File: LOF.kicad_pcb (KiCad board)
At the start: 2 copper layers, 29 parts, among them IC10 PEL12D-4225S-S1024, IC11 PEL12D-4225S-S1024, IC12 PEL12D-4225S-S1024, IC13 PEL12D-4225S-S1024, IC14 PEL12D-4225S-S1024, IC15 PEL12D-4225S-S1024, IC16 PEL12D-4225S-S1024, IC9 PEL12D-4225S-S1024

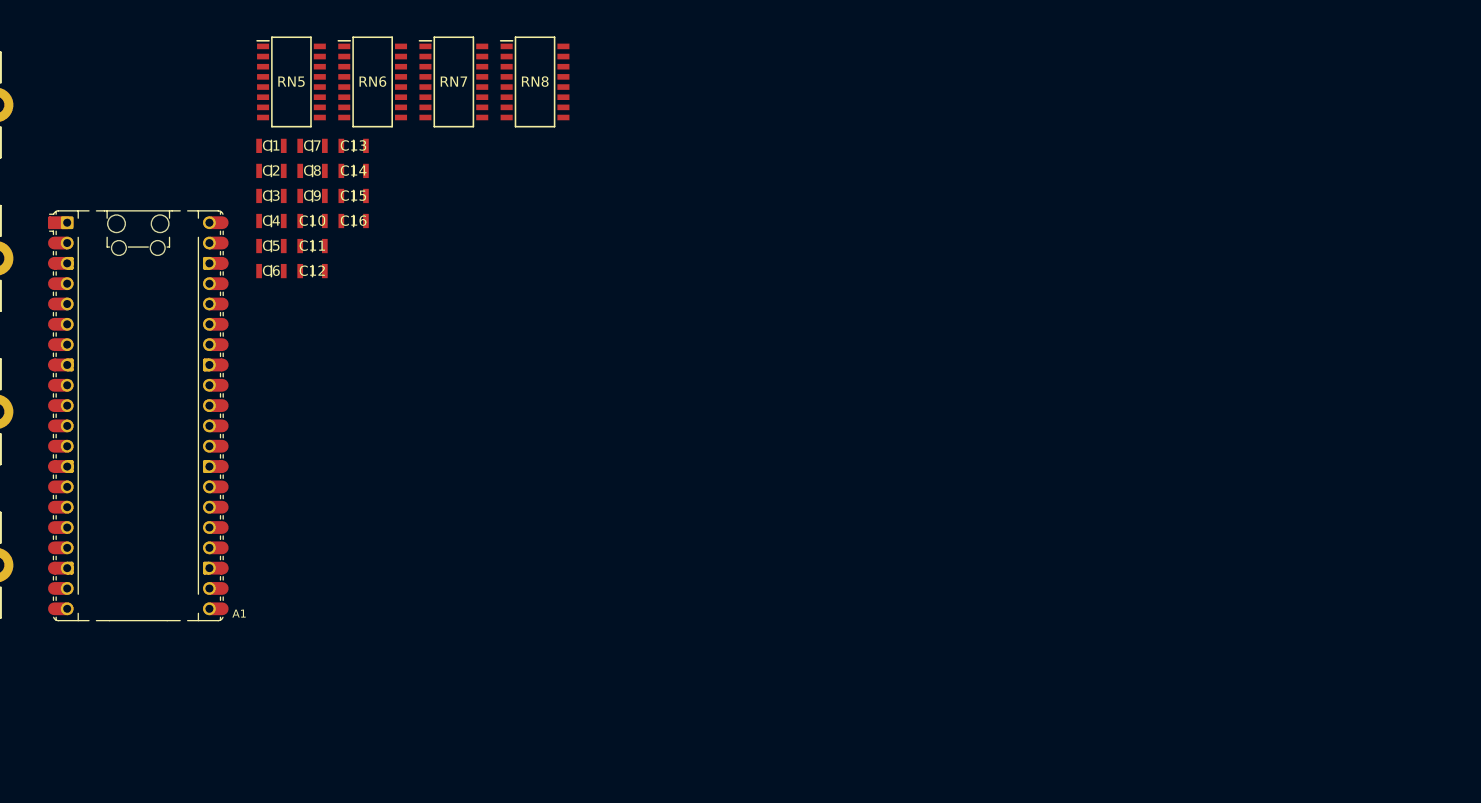
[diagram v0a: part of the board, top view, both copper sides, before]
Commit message: Added variable resistor and switches
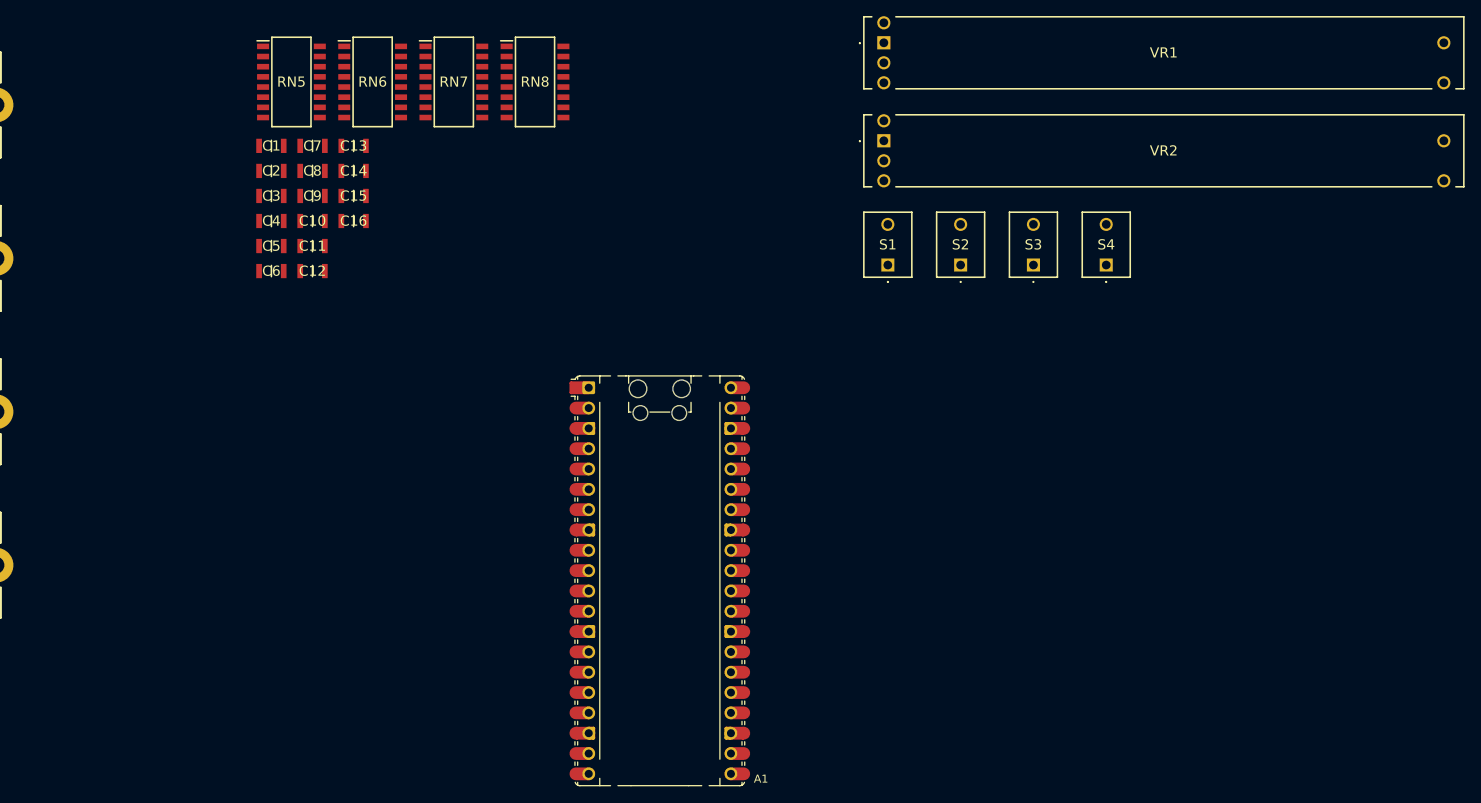
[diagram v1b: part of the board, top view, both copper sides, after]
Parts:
- added S1: 2MS6T1B3M2QES, SamacSys_Parts:2MS6T1B3M2QES, F.Cu at (196.5, 66.5)
- added S2: 2MS6T1B3M2QES, SamacSys_Parts:2MS6T1B3M2QES, F.Cu at (205.6, 66.5)
- added S3: 2MS6T1B3M2QES, SamacSys_Parts:2MS6T1B3M2QES, F.Cu at (214.7, 66.5)
- added S4: 2MS6T1B3M2QES, SamacSys_Parts:2MS6T1B3M2QES, F.Cu at (223.8, 66.5)
- added VR1: PTL60-15O1-104B2, SamacSys_Parts:PTL6015O1104B2, F.Cu at (196.0, 38.8)
- added VR2: PTL60-15O1-104B2, SamacSys_Parts:PTL6015O1104B2, F.Cu at (196.0, 51.0)
- moved A1 68.4 mm to (168.0, 106.0)
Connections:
- net 5V renamed /RC Filtered Encoders/5V
- IC10 pad 1: unconnected-(IC10---Pad1) -> GND
- IC10 pad 2: unconnected-(IC10-+_1-Pad2) -> /RC Filtered Encoders/E5_LED_BLUE
- IC10 pad 3: unconnected-(IC10-+_2-Pad3) -> /RC Filtered Encoders/E5_LED_ORANGE
- IC10 pad 4: unconnected-(IC10-COM-Pad4) -> /RC Filtered Encoders/E5_SW
- IC11 pad 1: unconnected-(IC11---Pad1) -> GND
- IC11 pad 2: unconnected-(IC11-+_1-Pad2) -> /RC Filtered Encoders/E2_LED_BLUE
- IC11 pad 3: unconnected-(IC11-+_2-Pad3) -> /RC Filtered Encoders/E2_LED_ORANGE
- IC11 pad 4: unconnected-(IC11-COM-Pad4) -> /RC Filtered Encoders/E2_SW
- IC12 pad 1: unconnected-(IC12---Pad1) -> GND
- IC12 pad 2: unconnected-(IC12-+_1-Pad2) -> /RC Filtered Encoders/E6_LED_BLUE
- IC12 pad 3: unconnected-(IC12-+_2-Pad3) -> /RC Filtered Encoders/E6_LED_ORANGE
- IC12 pad 4: unconnected-(IC12-COM-Pad4) -> /RC Filtered Encoders/E6_SW
- IC13 pad 1: unconnected-(IC13---Pad1) -> GND
- IC13 pad 2: unconnected-(IC13-+_1-Pad2) -> /RC Filtered Encoders/E3_LED_BLUE
- IC13 pad 3: unconnected-(IC13-+_2-Pad3) -> /RC Filtered Encoders/E3_LED_ORANGE
- IC13 pad 4: unconnected-(IC13-COM-Pad4) -> /RC Filtered Encoders/E3_SW
- IC14 pad 1: unconnected-(IC14---Pad1) -> GND
- IC14 pad 2: unconnected-(IC14-+_1-Pad2) -> /RC Filtered Encoders/E7_LED_BLUE
- IC14 pad 3: unconnected-(IC14-+_2-Pad3) -> /RC Filtered Encoders/E7_LED_ORANGE
- IC14 pad 4: unconnected-(IC14-COM-Pad4) -> /RC Filtered Encoders/E7_SW
- IC15 pad 1: unconnected-(IC15---Pad1) -> GND
- IC15 pad 2: unconnected-(IC15-+_1-Pad2) -> /RC Filtered Encoders/E4_LED_BLUE
- IC15 pad 3: unconnected-(IC15-+_2-Pad3) -> /RC Filtered Encoders/E4_LED_ORANGE
- IC15 pad 4: unconnected-(IC15-COM-Pad4) -> /RC Filtered Encoders/E4_SW
- IC16 pad 1: unconnected-(IC16---Pad1) -> GND
- IC16 pad 2: unconnected-(IC16-+_1-Pad2) -> /RC Filtered Encoders/E8_LED_BLUE
- IC16 pad 3: unconnected-(IC16-+_2-Pad3) -> /RC Filtered Encoders/E8_LED_ORANGE
- IC16 pad 4: unconnected-(IC16-COM-Pad4) -> /RC Filtered Encoders/E8_SW
- IC9 pad 1: unconnected-(IC9---Pad1) -> GND
- IC9 pad 2: unconnected-(IC9-+_1-Pad2) -> /RC Filtered Encoders/E1_LED_BLUE
- IC9 pad 3: unconnected-(IC9-+_2-Pad3) -> /RC Filtered Encoders/E1_LED_ORANGE
- IC9 pad 4: unconnected-(IC9-COM-Pad4) -> /RC Filtered Encoders/E1_SW

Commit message: Update schematic
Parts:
- added J1: EXT_3.3V, Connector_Wire:SolderWire-0.75sqmm_1x01_D1.25mm_OD3.5mm_Relief, F.Cu at (61.7, 160.7)
- added J2: VBUS_IN, Connector_Wire:SolderWire-0.75sqmm_1x01_D1.25mm_OD3.5mm_Relief, F.Cu at (67.7, 160.7)
- added J3: GND, Connector_Wire:SolderWire-0.75sqmm_1x01_D1.25mm_OD3.5mm_Relief, F.Cu at (73.8, 160.7)
- added U1: 815, Kicad Libs:MODULE_815, F.Cu at (90.6, 144.5)
- C1, C10, C11, C12, C13, C14, C15, C16, C2, C3, C4, C5, C6, C7, C8, C9: footprint SamacSys_Parts:CAPC3216X90N -> Kicad Libs:CAPC3216X90N
- IC10, IC11, IC12, IC13, IC14, IC15, IC16, IC9: footprint SamacSys_Parts:PEL12D4225SS1024 -> Kicad Libs:PEL12D4225SS1024
- S1, S2, S3, S4: footprint SamacSys_Parts:2MS6T1B3M2QES -> Kicad Libs:2MS6T1B3M2QES
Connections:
- net /RC Filtered Encoders/5V renamed /RC Filtered Encoders/3.3V
- net /RC Filtered Encoders/E1_SW renamed /E1_SW
- net /RC Filtered Encoders/E2_SW renamed /E2_SW
- net /RC Filtered Encoders/E3_SW renamed /E3_SW
- net /RC Filtered Encoders/E4_SW renamed /E4_SW
- net /RC Filtered Encoders/E5_SW renamed /E5_SW
- net /RC Filtered Encoders/E6_SW renamed /E6_SW
- net /RC Filtered Encoders/E7_SW renamed /E7_SW
- net /RC Filtered Encoders/E8_SW renamed /E8_SW
- A1 pad 1: unconnected-(A1-GPIO0-Pad1) -> /AOut1
- A1 pad 10: unconnected-(A1-GPIO7-Pad10) -> /BOut3
- A1 pad 11: unconnected-(A1-GPIO8-Pad11) -> /AOut4
- A1 pad 12: unconnected-(A1-GPIO9-Pad12) -> /BOut4
- A1 pad 14: unconnected-(A1-GPIO10-Pad14) -> /AOut5
- A1 pad 15: unconnected-(A1-GPIO11-Pad15) -> /BOut5
- A1 pad 16: unconnected-(A1-GPIO12-Pad16) -> /AOut6
- A1 pad 17: unconnected-(A1-GPIO13-Pad17) -> /BOut6
- A1 pad 19: unconnected-(A1-GPIO14-Pad19) -> /AOut7
- A1 pad 2: unconnected-(A1-GPIO1-Pad2) -> /BOut1
- A1 pad 20: unconnected-(A1-GPIO15-Pad20) -> /BOut7
- A1 pad 21: unconnected-(A1-GPIO16-Pad21) -> /AOut8
- A1 pad 22: unconnected-(A1-GPIO17-Pad22) -> /BOut8
- A1 pad 24: unconnected-(A1-GPIO18-Pad24) -> /S1_NC
- A1 pad 25: unconnected-(A1-GPIO19-Pad25) -> /S2_NC
- A1 pad 26: unconnected-(A1-GPIO20-Pad26) -> /S3_NC
- A1 pad 27: unconnected-(A1-GPIO21-Pad27) -> /S4_NC
- A1 pad 31: unconnected-(A1-GPIO26_ADC0-Pad31) -> /WIPER_VR1
- A1 pad 32: unconnected-(A1-GPIO27_ADC1-Pad32) -> /WIPER_VR2
- A1 pad 36: unconnected-(A1-3V3-Pad36) -> /3V3
- A1 pad 4: unconnected-(A1-GPIO2-Pad4) -> /AOut2
- A1 pad 40: unconnected-(A1-VBUS-Pad40) -> /VBUS
- A1 pad 5: unconnected-(A1-GPIO3-Pad5) -> /BOut2
- A1 pad 6: unconnected-(A1-GPIO4-Pad6) -> /SDA
- A1 pad 7: unconnected-(A1-GPIO5-Pad7) -> /SCL
- A1 pad 9: unconnected-(A1-GPIO6-Pad9) -> /AOut3
- C1 pad 1: /RC Filtered Encoders/C1_In -> /AOut1
- C10 pad 1: /RC Filtered Encoders/C10_In -> /BOut2
- C11 pad 1: /RC Filtered Encoders/C11_In -> /BOut3
- C12 pad 1: /RC Filtered Encoders/C12_In -> /BOut4
- C13 pad 1: /RC Filtered Encoders/C13_In -> /BOut5
- C14 pad 1: /RC Filtered Encoders/C14_In -> /BOut6
- C15 pad 1: /RC Filtered Encoders/C15_In -> /BOut7
- C16 pad 1: /RC Filtered Encoders/C16_In -> /BOut8
- C2 pad 1: /RC Filtered Encoders/C2_In -> /AOut2
- C3 pad 1: /RC Filtered Encoders/C3_In -> /AOut3
- C4 pad 1: /RC Filtered Encoders/C4_In -> /AOut4
- C5 pad 1: /RC Filtered Encoders/C5_In -> /AOut5
- C6 pad 1: /RC Filtered Encoders/C6_In -> /AOut6
- C7 pad 1: /RC Filtered Encoders/C7_In -> /AOut7
- C8 pad 1: /RC Filtered Encoders/C8_In -> /AOut8
- C9 pad 1: /RC Filtered Encoders/C9_In -> /BOut1
- IC10 pad 2: /RC Filtered Encoders/E5_LED_BLUE -> /E5_LED_BLUE
- IC10 pad 3: /RC Filtered Encoders/E5_LED_ORANGE -> /E5_LED_ORANGE
- IC10 pad A1: /RC Filtered Encoders/C5_In -> /AOut5
- IC10 pad B1: /RC Filtered Encoders/C13_In -> /BOut5
- IC11 pad 2: /RC Filtered Encoders/E2_LED_BLUE -> /E2_LED_BLUE
- IC11 pad 3: /RC Filtered Encoders/E2_LED_ORANGE -> /E2_LED_ORANGE
- IC11 pad A1: /RC Filtered Encoders/C2_In -> /AOut2
- IC11 pad B1: /RC Filtered Encoders/C10_In -> /BOut2
- IC12 pad 2: /RC Filtered Encoders/E6_LED_BLUE -> /E6_LED_BLUE
- IC12 pad 3: /RC Filtered Encoders/E6_LED_ORANGE -> /E6_LED_ORANGE
- IC12 pad A1: /RC Filtered Encoders/C6_In -> /AOut6
- IC12 pad B1: /RC Filtered Encoders/C14_In -> /BOut6
- IC13 pad 2: /RC Filtered Encoders/E3_LED_BLUE -> /E3_LED_BLUE
- IC13 pad 3: /RC Filtered Encoders/E3_LED_ORANGE -> /E3_LED_ORANGE
- IC13 pad A1: /RC Filtered Encoders/C3_In -> /AOut3
- IC13 pad B1: /RC Filtered Encoders/C11_In -> /BOut3
- IC14 pad 2: /RC Filtered Encoders/E7_LED_BLUE -> /E7_LED_BLUE
- IC14 pad 3: /RC Filtered Encoders/E7_LED_ORANGE -> /E7_LED_ORANGE
- IC14 pad A1: /RC Filtered Encoders/C7_In -> /AOut7
- IC14 pad B1: /RC Filtered Encoders/C15_In -> /BOut7
- IC15 pad 2: /RC Filtered Encoders/E4_LED_BLUE -> /E4_LED_BLUE
- IC15 pad 3: /RC Filtered Encoders/E4_LED_ORANGE -> /E4_LED_ORANGE
- IC15 pad A1: /RC Filtered Encoders/C4_In -> /AOut4
- IC15 pad B1: /RC Filtered Encoders/C12_In -> /BOut4
- IC16 pad 2: /RC Filtered Encoders/E8_LED_BLUE -> /E8_LED_BLUE
- IC16 pad 3: /RC Filtered Encoders/E8_LED_ORANGE -> /E8_LED_ORANGE
- IC16 pad A1: /RC Filtered Encoders/C8_In -> /AOut8
- IC16 pad B1: /RC Filtered Encoders/C16_In -> /BOut8
- IC9 pad 2: /RC Filtered Encoders/E1_LED_BLUE -> /E1_LED_BLUE
- IC9 pad 3: /RC Filtered Encoders/E1_LED_ORANGE -> /E1_LED_ORANGE
- IC9 pad A1: /RC Filtered Encoders/C1_In -> /AOut1
- IC9 pad B1: /RC Filtered Encoders/C9_In -> /BOut1
- RN5 pad 10: /RC Filtered Encoders/C7_In -> /AOut7
- RN5 pad 11: /RC Filtered Encoders/C6_In -> /AOut6
- RN5 pad 12: /RC Filtered Encoders/C5_In -> /AOut5
- RN5 pad 13: /RC Filtered Encoders/C4_In -> /AOut4
- RN5 pad 14: /RC Filtered Encoders/C3_In -> /AOut3
- RN5 pad 15: /RC Filtered Encoders/C2_In -> /AOut2
- RN5 pad 16: /RC Filtered Encoders/C1_In -> /AOut1
- RN5 pad 9: /RC Filtered Encoders/C8_In -> /AOut8
- RN6 pad 10: /RC Filtered Encoders/C15_In -> /BOut7
- RN6 pad 11: /RC Filtered Encoders/C14_In -> /BOut6
- RN6 pad 12: /RC Filtered Encoders/C13_In -> /BOut5
- RN6 pad 13: /RC Filtered Encoders/C12_In -> /BOut4
- RN6 pad 14: /RC Filtered Encoders/C11_In -> /BOut3
- RN6 pad 15: /RC Filtered Encoders/C10_In -> /BOut2
- RN6 pad 16: /RC Filtered Encoders/C9_In -> /BOut1
- RN6 pad 9: /RC Filtered Encoders/C16_In -> /BOut8
- RN7 pad 1: /RC Filtered Encoders/C1_In -> /AOut1
- RN7 pad 10: /RC Filtered Encoders/C7_In -> /AOut7
- RN7 pad 11: /RC Filtered Encoders/C6_In -> /AOut6
- RN7 pad 12: /RC Filtered Encoders/C5_In -> /AOut5
- RN7 pad 13: /RC Filtered Encoders/C4_In -> /AOut4
- RN7 pad 14: /RC Filtered Encoders/C3_In -> /AOut3
- RN7 pad 15: /RC Filtered Encoders/C2_In -> /AOut2
- RN7 pad 16: /RC Filtered Encoders/C1_In -> /AOut1
- RN7 pad 2: /RC Filtered Encoders/C2_In -> /AOut2
- RN7 pad 3: /RC Filtered Encoders/C3_In -> /AOut3
- RN7 pad 4: /RC Filtered Encoders/C4_In -> /AOut4
- RN7 pad 5: /RC Filtered Encoders/C5_In -> /AOut5
- RN7 pad 6: /RC Filtered Encoders/C6_In -> /AOut6
- RN7 pad 7: /RC Filtered Encoders/C7_In -> /AOut7
- RN7 pad 8: /RC Filtered Encoders/C8_In -> /AOut8
- RN7 pad 9: /RC Filtered Encoders/C8_In -> /AOut8
- RN8 pad 1: /RC Filtered Encoders/C9_In -> /BOut1
- RN8 pad 10: /RC Filtered Encoders/C15_In -> /BOut7
- RN8 pad 11: /RC Filtered Encoders/C14_In -> /BOut6
- RN8 pad 12: /RC Filtered Encoders/C13_In -> /BOut5
- RN8 pad 13: /RC Filtered Encoders/C12_In -> /BOut4
- RN8 pad 14: /RC Filtered Encoders/C11_In -> /BOut3
- RN8 pad 15: /RC Filtered Encoders/C10_In -> /BOut2
- RN8 pad 16: /RC Filtered Encoders/C9_In -> /BOut1
- RN8 pad 2: /RC Filtered Encoders/C10_In -> /BOut2
- RN8 pad 3: /RC Filtered Encoders/C11_In -> /BOut3
- RN8 pad 4: /RC Filtered Encoders/C12_In -> /BOut4
- RN8 pad 5: /RC Filtered Encoders/C13_In -> /BOut5
- RN8 pad 6: /RC Filtered Encoders/C14_In -> /BOut6
- RN8 pad 7: /RC Filtered Encoders/C15_In -> /BOut7
- RN8 pad 8: /RC Filtered Encoders/C16_In -> /BOut8
- RN8 pad 9: /RC Filtered Encoders/C16_In -> /BOut8
- S1 pad 1: unconnected-(S1-NO-Pad1) -> GND
- S2 pad 1: unconnected-(S2-NO-Pad1) -> GND
- S3 pad 1: unconnected-(S3-NO-Pad1) -> GND
- S4 pad 1: unconnected-(S4-NO-Pad1) -> GND
- VR1 pad 1: unconnected-(VR1-CCW-Pad1) -> GND
- VR1 pad 2: unconnected-(VR1-WIPER-Pad2) -> /WIPER_VR1
- VR1 pad 3: unconnected-(VR1-CW-Pad3) -> +3.3V
- VR1 pad B1: unconnected-(VR1-B_(+)-PadB1) -> /EXT_3.3V
- VR1 pad E1: unconnected-(VR1-E_(-)-PadE1) -> GND
- VR2 pad 1: unconnected-(VR2-CCW-Pad1) -> GND
- VR2 pad 2: unconnected-(VR2-WIPER-Pad2) -> /WIPER_VR2
- VR2 pad 3: unconnected-(VR2-CW-Pad3) -> +3.3V
- VR2 pad B1: unconnected-(VR2-B_(+)-PadB1) -> /EXT_3.3V
- VR2 pad E1: unconnected-(VR2-E_(-)-PadE1) -> GND

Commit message: Made fixes according to the erc
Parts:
- removed U1: 815, Kicad Libs:MODULE_815
- added J10: Conn_01x01, Connector_Wire:SolderWire-0.25sqmm_1x01_D0.65mm_OD1.7mm, F.Cu at (45.8, 169.9)
- added J11: Conn_01x01, Connector_Wire:SolderWire-0.25sqmm_1x01_D0.65mm_OD1.7mm, F.Cu at (45.8, 173.8)
- added J12: Conn_01x01, Connector_Wire:SolderWire-0.25sqmm_1x01_D0.65mm_OD1.7mm, F.Cu at (45.8, 177.7)
- added J13: Conn_01x01, Connector_Wire:SolderWire-0.25sqmm_1x01_D0.65mm_OD1.7mm, F.Cu at (50.0, 158.2)
- added J14: Conn_01x01, Connector_Wire:SolderWire-0.25sqmm_1x01_D0.65mm_OD1.7mm, F.Cu at (50.0, 162.1)
- added J15: Conn_01x01, Connector_Wire:SolderWire-0.25sqmm_1x01_D0.65mm_OD1.7mm, F.Cu at (50.0, 166.0)
- added J16: Conn_01x01, Connector_Wire:SolderWire-0.25sqmm_1x01_D0.65mm_OD1.7mm, F.Cu at (50.0, 169.9)
- added J17: Conn_01x01, Connector_Wire:SolderWire-0.25sqmm_1x01_D0.65mm_OD1.7mm, F.Cu at (50.0, 173.8)
- added J18: Conn_01x01, Connector_Wire:SolderWire-0.25sqmm_1x01_D0.65mm_OD1.7mm, F.Cu at (50.0, 177.7)
- added J19: Conn_01x01, Connector_Wire:SolderWire-0.25sqmm_1x01_D0.65mm_OD1.7mm, F.Cu at (54.2, 162.1)
- added J20: Conn_01x01, Connector_Wire:SolderWire-0.25sqmm_1x01_D0.65mm_OD1.7mm, F.Cu at (54.2, 166.0)
- added J21: Conn_01x01, Connector_Wire:SolderWire-0.25sqmm_1x01_D0.65mm_OD1.7mm, F.Cu at (54.2, 169.9)
- added J22: Conn_01x01, Connector_Wire:SolderWire-0.25sqmm_1x01_D0.65mm_OD1.7mm, F.Cu at (54.2, 158.2)
- added J23: Conn_01x01, Connector_Wire:SolderWire-0.25sqmm_1x01_D0.65mm_OD1.7mm, F.Cu at (34.5, 36.5)
- added J24: Conn_01x01, Connector_Wire:SolderWire-0.25sqmm_1x01_D0.65mm_OD1.7mm, F.Cu at (34.5, 42.0)
- added J25: Conn_01x01, Connector_Wire:SolderWire-0.25sqmm_1x01_D0.65mm_OD1.7mm, F.Cu at (34.0, 48.0)
- added J4: Conn_01x01, Connector_Wire:SolderWire-0.25sqmm_1x01_D0.65mm_OD1.7mm, F.Cu at (41.5, 169.9)
- added J5: Conn_01x01, Connector_Wire:SolderWire-0.25sqmm_1x01_D0.65mm_OD1.7mm, F.Cu at (41.5, 173.8)
- added J6: Conn_01x01, Connector_Wire:SolderWire-0.25sqmm_1x01_D0.65mm_OD1.7mm, F.Cu at (41.5, 177.7)
- added J7: Conn_01x01, Connector_Wire:SolderWire-0.25sqmm_1x01_D0.65mm_OD1.7mm, F.Cu at (45.8, 158.2)
- added J8: Conn_01x01, Connector_Wire:SolderWire-0.25sqmm_1x01_D0.65mm_OD1.7mm, F.Cu at (45.8, 162.1)
- added J9: Conn_01x01, Connector_Wire:SolderWire-0.25sqmm_1x01_D0.65mm_OD1.7mm, F.Cu at (45.8, 166.0)
- J1: value EXT_3.3V -> Conn_01x01; footprint Connector_Wire:SolderWire-0.75sqmm_1x01_D1.25mm_OD3.5mm_Relief -> Connector_Wire:SolderWire-0.25sqmm_1x01_D0.65mm_OD1.7mm
- J2: value VBUS_IN -> Conn_01x01; footprint Connector_Wire:SolderWire-0.75sqmm_1x01_D1.25mm_OD3.5mm_Relief -> Connector_Wire:SolderWire-0.25sqmm_1x01_D0.65mm_OD1.7mm
- J3: value GND -> Conn_01x01; footprint Connector_Wire:SolderWire-0.75sqmm_1x01_D1.25mm_OD3.5mm_Relief -> Connector_Wire:SolderWire-0.25sqmm_1x01_D0.65mm_OD1.7mm
- moved J3 32.7 mm to (41.5, 166.0)
- moved J2 26.3 mm to (41.5, 162.1)
- moved A1 24.7 mm to (145.0, 115.0)
- moved J1 20.3 mm to (41.5, 158.2)
- moved S1 0.50 mm to (196.0, 66.5)
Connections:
- A1 pad 13: Net-(A1-GND-Pad13) -> unconnected-(A1-GND-Pad13)_9
- A1 pad 18: Net-(A1-GND-Pad13) -> unconnected-(A1-GND-Pad13)_1
- A1 pad 23: Net-(A1-GND-Pad13) -> unconnected-(A1-GND-Pad13)_13
- A1 pad 24: /S1_NC -> /GPIO18
- A1 pad 25: /S2_NC -> /GPIO19
- A1 pad 26: /S3_NC -> /GPIO20
- A1 pad 27: /S4_NC -> /GPIO21
- A1 pad 28: Net-(A1-GND-Pad13) -> unconnected-(A1-GND-Pad13)_3
- A1 pad 29: unconnected-(A1-GPIO22-Pad29) -> /OE
- A1 pad 3: Net-(A1-GND-Pad13) -> unconnected-(A1-GND-Pad13)_6
- A1 pad 33: unconnected-(A1-AGND-Pad33) -> GND
- A1 pad 38: Net-(A1-GND-Pad13) -> unconnected-(A1-GND-Pad13)_10
- A1 pad 8: Net-(A1-GND-Pad13) -> unconnected-(A1-GND-Pad13)_2
- IC10 pad 2: /E5_LED_BLUE -> /PWM_9
- IC10 pad 3: /E5_LED_ORANGE -> /PWM_8
- IC10 pad 4: /E5_SW -> GND
- IC11 pad 2: /E2_LED_BLUE -> /PWM_3
- IC11 pad 3: /E2_LED_ORANGE -> /PWM_2
- IC11 pad 4: /E2_SW -> GND
- IC12 pad 2: /E6_LED_BLUE -> /PWM_10
- IC12 pad 3: /E6_LED_ORANGE -> /PWM_11
- IC12 pad 4: /E6_SW -> GND
- IC13 pad 2: /E3_LED_BLUE -> /PWM_5
- IC13 pad 3: /E3_LED_ORANGE -> /PWM_4
- IC13 pad 4: /E3_SW -> GND
- IC14 pad 2: /E7_LED_BLUE -> /PWM_12
- IC14 pad 3: /E7_LED_ORANGE -> /PWM_13
- IC14 pad 4: /E7_SW -> GND
- IC15 pad 2: /E4_LED_BLUE -> /PWM_7
- IC15 pad 3: /E4_LED_ORANGE -> /PWM_6
- IC15 pad 4: /E4_SW -> GND
- IC16 pad 2: /E8_LED_BLUE -> /PWM_15
- IC16 pad 3: /E8_LED_ORANGE -> /PWM_14
- IC16 pad 4: /E8_SW -> GND
- IC9 pad 2: /E1_LED_BLUE -> /PWM_1
- IC9 pad 3: /E1_LED_ORANGE -> /PWM_0
- IC9 pad 4: /E1_SW -> GND
- J1 pad 1: /EXT_3.3V -> /3V3
- J2 pad 1: unconnected-(J2-Pin_1-Pad1) -> /LED_VCC
- J3 pad 1: GND -> /PWM_0
- RN5 pad 1: /RC Filtered Encoders/3.3V -> /3V3
- RN5 pad 2: /RC Filtered Encoders/3.3V -> /3V3
- RN5 pad 3: /RC Filtered Encoders/3.3V -> /3V3
- RN5 pad 4: /RC Filtered Encoders/3.3V -> /3V3
- RN5 pad 5: /RC Filtered Encoders/3.3V -> /3V3
- RN5 pad 6: /RC Filtered Encoders/3.3V -> /3V3
- RN5 pad 7: /RC Filtered Encoders/3.3V -> /3V3
- RN5 pad 8: /RC Filtered Encoders/3.3V -> /3V3
- RN6 pad 1: /RC Filtered Encoders/3.3V -> /3V3
- RN6 pad 2: /RC Filtered Encoders/3.3V -> /3V3
- RN6 pad 3: /RC Filtered Encoders/3.3V -> /3V3
- RN6 pad 4: /RC Filtered Encoders/3.3V -> /3V3
- RN6 pad 5: /RC Filtered Encoders/3.3V -> /3V3
- RN6 pad 6: /RC Filtered Encoders/3.3V -> /3V3
- RN6 pad 7: /RC Filtered Encoders/3.3V -> /3V3
- RN6 pad 8: /RC Filtered Encoders/3.3V -> /3V3
- S1 pad 3: unconnected-(S1-NC-Pad3) -> /GPIO18
- S2 pad 3: unconnected-(S2-NC-Pad3) -> /GPIO19
- S3 pad 3: unconnected-(S3-NC-Pad3) -> /GPIO20
- S4 pad 3: unconnected-(S4-NC-Pad3) -> /GPIO21
- VR1 pad 3: +3.3V -> /3V3
- VR1 pad B1: /EXT_3.3V -> /LED_VCC
- VR1 pad L1: unconnected-(VR1-DUMMY_TERMINAL-PadL1) -> GND
- VR2 pad 3: +3.3V -> /3V3
- VR2 pad B1: /EXT_3.3V -> /LED_VCC
- VR2 pad L1: unconnected-(VR2-DUMMY_TERMINAL-PadL1) -> GND

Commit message: All components and footprints set
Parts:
- added R1: R, Resistor_THT:R_Axial_DIN0207_L6.3mm_D2.5mm_P10.16mm_Horizontal, F.Cu at (-73.9, 131.9)
- added R2: R, Resistor_THT:R_Axial_DIN0207_L6.3mm_D2.5mm_P10.16mm_Horizontal, F.Cu at (-73.9, 136.0)
- added RN9: 4816P-T01-103LF, SamacSys_Parts:SOIC127P762X215-16N, F.Cu at (300.5, -19.1)
- S1, S2, S3, S4: footprint Kicad Libs:2MS6T1B3M2QES -> SamacSys_Parts:2MS6T1B3M2QES
- moved C13 201.3 mm to (321.0, -11.2)
- moved C14 201.3 mm to (321.0, -8.05)
- moved C15 201.3 mm to (321.0, -4.92)
- moved C16 201.3 mm to (321.0, -1.79)
- moved RN6 201.3 mm to (323.4, -19.2)
- moved C1 201.3 mm to (310.7, -11.2)
- moved C10 201.3 mm to (315.9, -1.79)
- moved C11 201.3 mm to (315.9, 1.33)
- moved C12 201.3 mm to (315.9, 4.46)
- moved C2 201.3 mm to (310.7, -8.05)
- moved C3 201.3 mm to (310.7, -4.92)
- moved C4 201.3 mm to (310.7, -1.79)
- moved C5 201.3 mm to (310.7, 1.33)
- moved C6 201.3 mm to (310.7, 4.46)
- moved C7 201.3 mm to (315.9, -11.2)
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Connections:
- VR1 pad B1: /LED_VCC -> Net-(VR1-B_(+))
- VR2 pad B1: /LED_VCC -> Net-(VR2-B_(+))
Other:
- copper layers 2 -> 4
